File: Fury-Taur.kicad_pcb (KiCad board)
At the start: 2 copper layers, 78 x 25 mm, 29 parts, among them J1 Pickup, J2 Output, Q1 Bias 20K, Q1 J201, Q2 Bias 20K, Q2 J201, SW1 ALPHA_PUSH_PULL, SW2 SW_SPDT

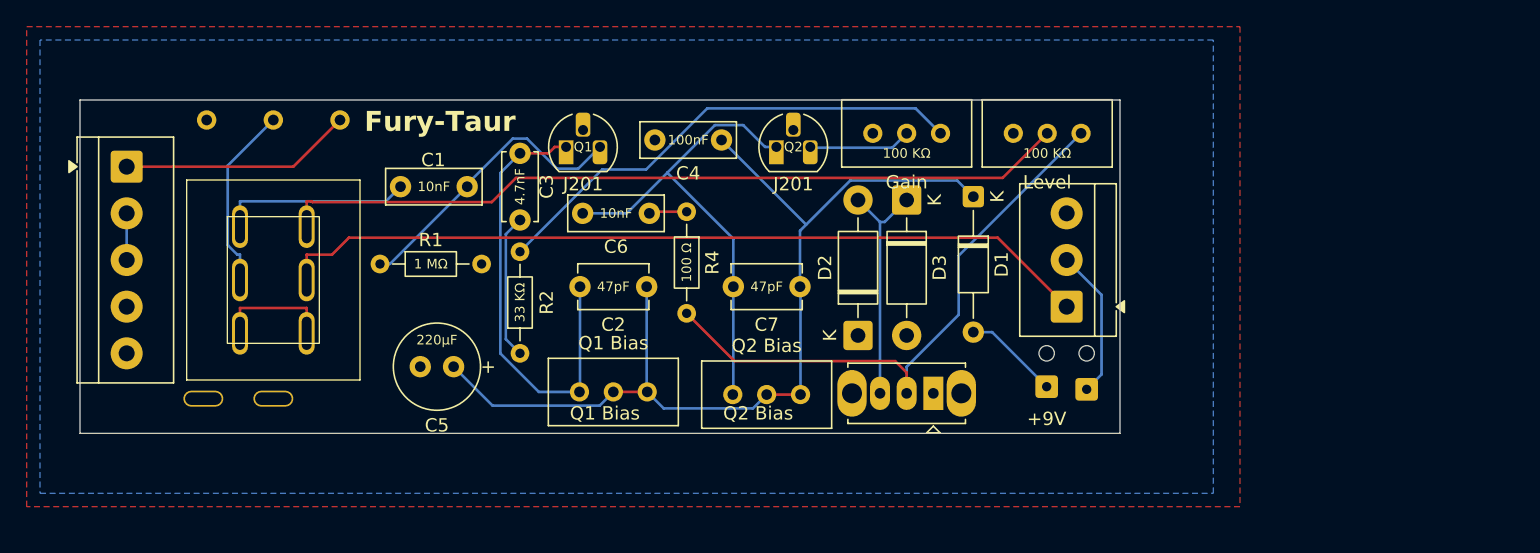
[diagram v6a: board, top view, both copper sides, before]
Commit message: Slight reaaranging of parts for cleaner board
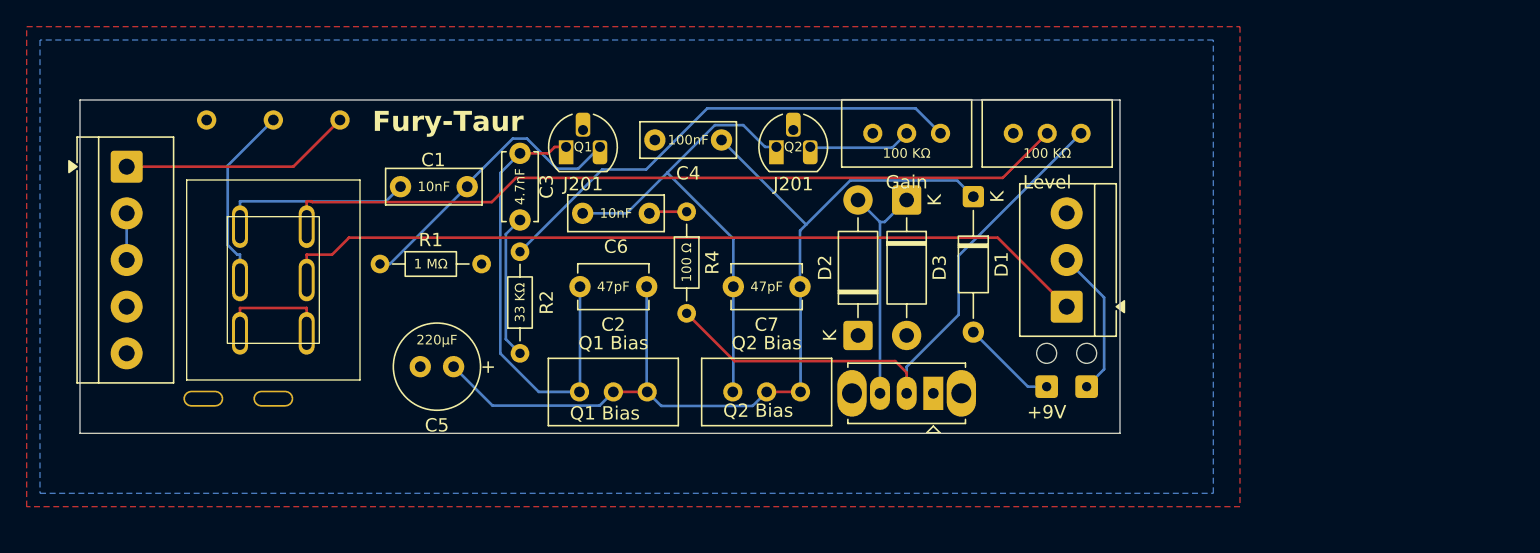
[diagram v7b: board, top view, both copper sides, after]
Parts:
- removed 9V-: SolderWire-0.127sqmm_1x01_D0.48mm_OD1mm, Connector_Wire:SolderWire-0.127sqmm_1x01_D0.48mm_OD1mm
- added BAT-: SolderWire-0.127sqmm_1x01_D0.48mm_OD1mm, Connector_Wire:SolderWire-0.127sqmm_1x01_D0.48mm_OD1mm, F.Cu at (154.0, 85.5)
- moved Q2 Bias 0.20 mm to (132.5, 85.9)

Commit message: Adjusted bias pots
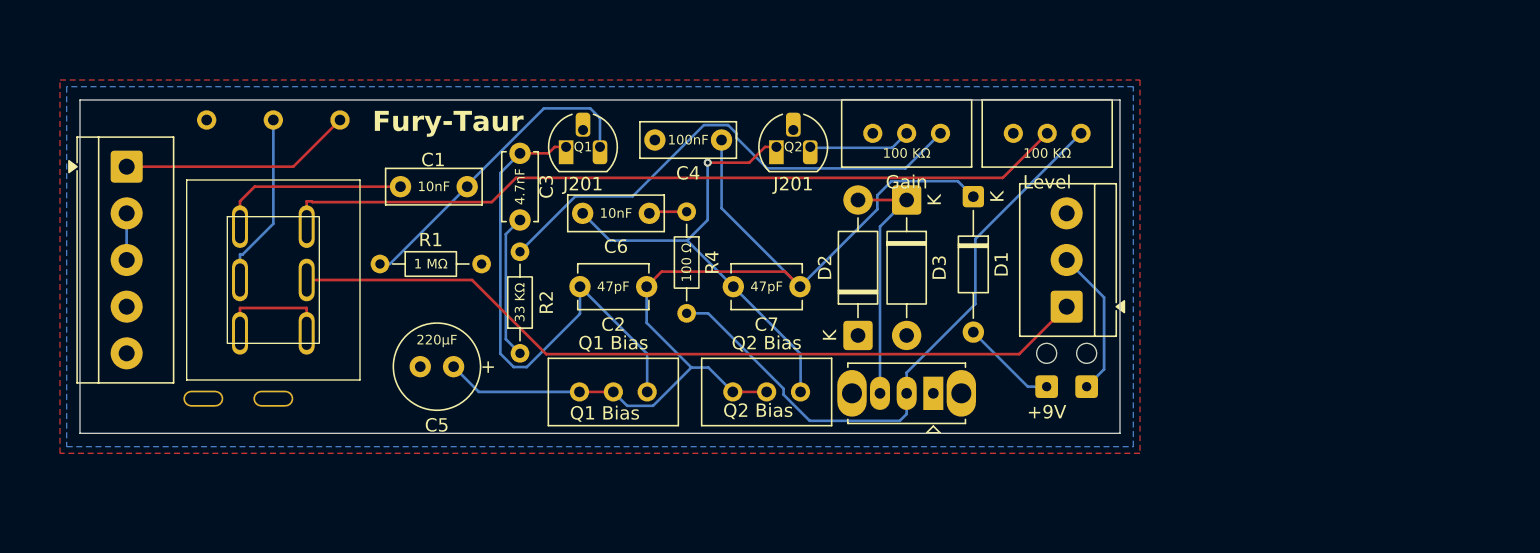
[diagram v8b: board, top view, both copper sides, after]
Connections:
- Q1 Bias pad 1: Net-(D1-K) -> Net-(Q1-D)
- Q1 Bias pad 3: Net-(Q1-D) -> Net-(D1-K)
- Q2 Bias pad 1: Net-(D1-K) -> Net-(Q2-D)
- Q2 Bias pad 3: Net-(Q2-D) -> Net-(D1-K)
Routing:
- net Net-(Q1-D): track 34.3 -> 39.4 mm
- net Net-(D1-K): track 72.6 -> 77.3 mm
- net Net-(SW2-B): track 44.8 -> 46.8 mm
- net Net-(Q1-G): track 22.1 -> 23.9 mm
- net Net-(R2-Pad2): track 36.8 -> 38.1 mm
- net Net-(D2-A): track 17.9 -> 19.0 mm
- net VOL_OUT_TO_JACK_TIP: track 61.6 -> 60.8 mm
- net Net-(Q2-D): track 36.5 -> 35.7 mm, vias 0 -> 1
- net VOL_OUT_TO_SWITCH: track 13.9 -> 13.1 mm
